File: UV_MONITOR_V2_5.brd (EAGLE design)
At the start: 160 x 100 mm, 33 parts, among them U2 LM2903M, U3 MCP7940N-I/SN, U4 ML8511 UV_SENSOR, U9 MIC5219 3.3V, Y1 32.768kHz

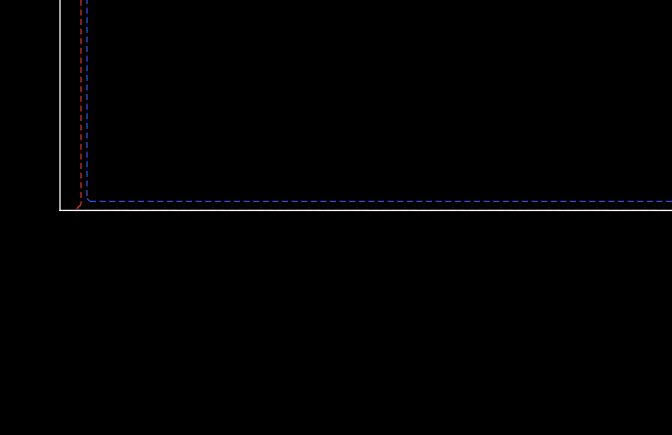
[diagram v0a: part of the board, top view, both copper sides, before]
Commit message: minor edits
Created some edits for my own benefit. These edits were to an old version of our schematic and board.
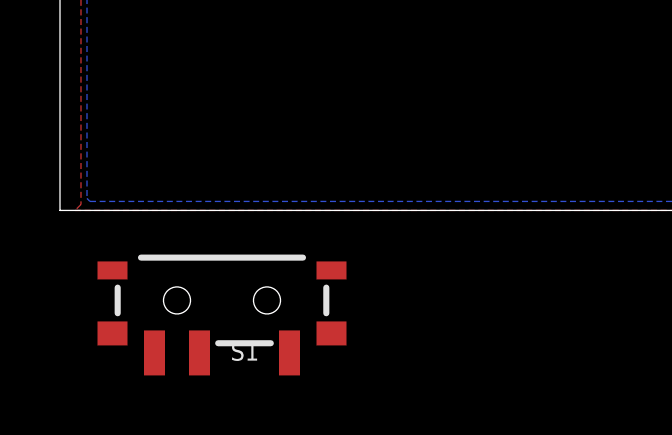
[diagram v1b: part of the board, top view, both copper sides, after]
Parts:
- added S1: (no value), SparkFun-Switches:SWITCH_SPST_SMD_A
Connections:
- new net N$11: C3.1, S1.1, U$3.VBAT1, U$3.VBAT2
- net MAIN_BAT: now also S1.2; no longer C3.1, U$3.VBAT1, U$3.VBAT2
- net VBUS: now also S1.3
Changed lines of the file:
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@@
 </element>
 <element name="U$6" library="SP0503BAHT" package="SP0503BAHT" value="SP0503BAHT" x="113.9" y="84.6"/>
+<element name="S1" library="SparkFun-Switches" library_urn="urn:adsk.eagle:library:535" package="SWITCH_SPST_SMD_A" package3d_urn="urn:adsk.eagle:package:40179/1" value="" x="5.4" y="-3">
+<attribute name="PROD_ID" value="SWCH-10651" x="5.4" y="-3" size="1.778" layer="27" display="off"/>
+<attribute name="SF_SKU" value="COM-10860" x="5.4" y="-3" size="1.778" layer="27" display="off"/>
+</element>
 </elements>
 <signals>
@@
 </signal>
 <signal name="MAIN_BAT">
-<contactref element="C3" pad="1"/>
 <contactref element="R1" pad="1"/>
 <contactref element="U9" pad="1"/>
-<contactref element="U$3" pad="VBAT1"/>
-<contactref element="U$3" pad="VBAT2"/>
-<wire x1="149.82" y1="52.75" x2="153.6" y2="51.4" width="0" layer="19" extent="1-16"/>
-<wire x1="148.72" y1="47.29" x2="149.82" y2="52.75" width="0" layer="19" extent="1-1"/>
-<wire x1="144.7001" y1="49.55" x2="148.72" y2="47.29" width="0" layer="19" extent="1-1"/>
-<wire x1="140.6" y1="51.4" x2="144.7001" y2="49.55" width="0" layer="19" extent="1-16"/>
+<contactref element="S1" pad="2"/>
+<wire x1="144.7001" y1="49.55" x2="149.82" y2="52.75" width="0" layer="19" extent="1-1"/>
+<wire x1="4.65" y1="-4.75" x2="144.7001" y2="49.55" width="0" layer="19" extent="1-1"/>
 </signal>
 <signal name="EN">
@@
 <contactref element="U$1" pad="VREGIN"/>
 <contactref element="U$6" pad="P$4"/>
+<contactref element="S1" pad="3"/>
 <wire x1="114.85" y1="83.5" x2="114.6" y2="89.025" width="0" layer="19" extent="1-1"/>
 <wire x1="115.5" y1="81.4" x2="114.85" y2="83.5" width="0" layer="19" extent="1-1"/>
 <wire x1="116.4" y1="80.5" x2="115.5" y2="81.4" width="0" layer="19" extent="1-1"/>
+<wire x1="7.65" y1="-4.75" x2="115.5" y2="81.4" width="0" layer="19" extent="1-1"/>
 </signal>
 <signal name="D-">
@@
 <wire x1="114.5" y1="76.6" x2="108.5" y2="84.5" width="0" layer="19" extent="1-1"/>
 </signal>
+<signal name="N$11">
+<contactref element="C3" pad="1"/>
+<contactref element="U$3" pad="VBAT1"/>
+<contactref element="U$3" pad="VBAT2"/>
+<contactref element="S1" pad="1"/>
+<wire x1="148.72" y1="47.29" x2="153.6" y2="51.4" width="0" layer="19" extent="1-16"/>
+<wire x1="140.6" y1="51.4" x2="148.72" y2="47.29" width="0" layer="19" extent="1-16"/>
+<wire x1="3.15" y1="-4.75" x2="140.6" y2="51.4" width="0" layer="19" extent="1-16"/>
+</signal>
 </signals>
